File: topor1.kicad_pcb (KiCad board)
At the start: 2 copper layers, 99.8 x 99.8 mm, 76 parts, among them IC1 ATMEGA168-A, P1 CONN_01X02_PWR, P2 USB_B, P3 CONN_02X13_X0, P4 CONN_02X13_X3, P5 CONN_02X13_X1, P6 JTAG CONN_02X07_JTAG, U1 AP1117_ADJ, U2 AP1117_33, U3 AP1117_ADJ, U4 FT232RL, U5 M25P16-VME, U6 ECS-3963, U7 XC6SLX9-TQG144, Y1 11.059MHz

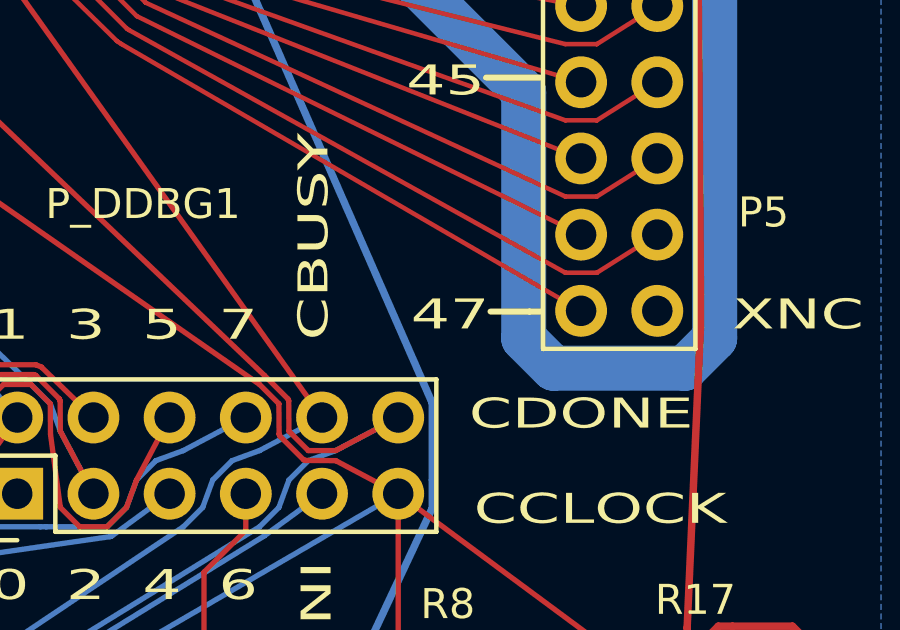
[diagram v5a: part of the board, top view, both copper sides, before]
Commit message: correction in silkscreen
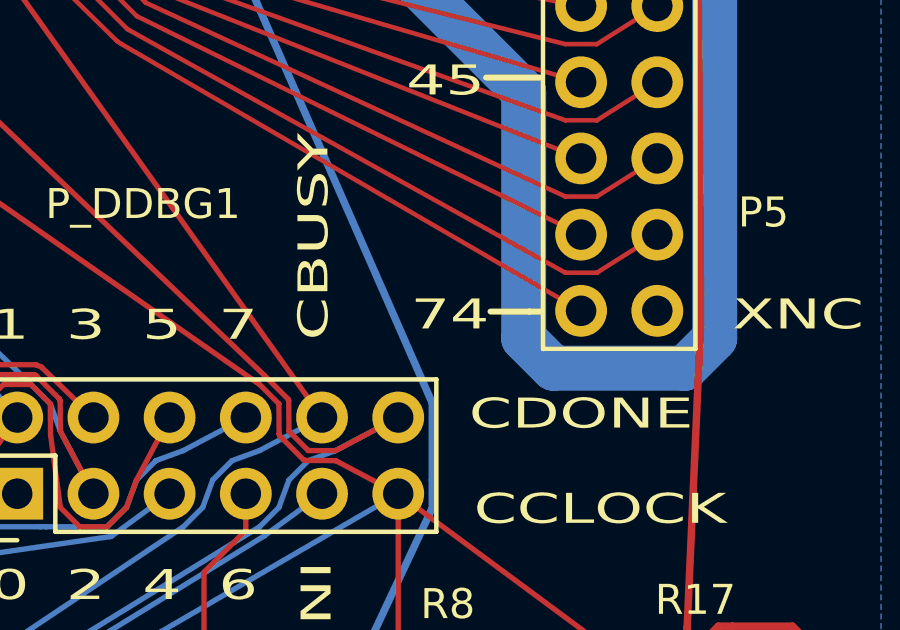
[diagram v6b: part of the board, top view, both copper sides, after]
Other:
- board text added: "74"
- board text removed: "47"
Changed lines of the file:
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@@
     (effects (font (size 1 1.5) (thickness 0.25)))
   )
-  (gr_text 47 (at 149.3 125.6) (layer F.SilkS)
+  (gr_text 74 (at 149.3 125.6) (layer F.SilkS)
     (effects (font (size 1 1.5) (thickness 0.25)))
   )
